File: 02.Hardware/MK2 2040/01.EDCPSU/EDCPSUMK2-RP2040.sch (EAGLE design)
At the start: 185 parts, among them J1 DX07S016JA1R1500, J6 Display, K1 FLEX CONNECTORES, Q2 2N7002PW, Q4 2N7002PW, Q5 2N7002PW, Q9 2N7002PW, U1 RP2040TR7, U10 IP2721, U11 AP63203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

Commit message: Añadido Test Pads
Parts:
- added 3V3MCU, EN_TPS54531, GND, GND_IN, IN+, ISENSE, N$41, N$51, N$59, OVC_ALARM, PEDAL+, PEDAL-, RUN, SCL, SDA, SEL, SWCLK, SWDIO, USB-D+, USB-D-, VBUS_SENSE, VOSEN, VOUT: TESTPAD_TPSQB1,27, BeagleBone_Blue_R3:TESTPAD_TPSQB1,27
- R35: value 330R -> 130R
- R36: value 75K -> 27K
- R51: value 220K -> 390K
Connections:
- net 3V3MCU: now also 3V3MCU.TP
- net EN_TPS54531: now also EN_TPS54531.TP
- net GND: now also GND.TP
- net GND_IN: now also GND_IN.TP
- net IN+: now also IN+.TP
- net ISENSE: now also ISENSE.TP
- net N$41: now also N$41.TP
- net N$51: now also N$51.TP
- net N$59: now also N$59.TP
- net OVC_ALARM: now also OVC_ALARM.TP
- net PEDAL+: now also PEDAL+.TP
- net PEDAL-: now also PEDAL-.TP
- net RUN: now also RUN.TP
- net SCL: now also SCL.TP
- net SDA: now also SDA.TP
- net SEL: now also SEL.TP
- net SWCLK: now also SWCLK.TP
- net SWDIO: now also SWDIO.TP
- net USB_D+: now also USB-D+.TP
- net USB_D-: now also USB-D-.TP
- net VBUS_SENSE: now also VBUS_SENSE.TP
- net VOSEN: now also VOSEN.TP
- net VOUT: now also VOUT.TP
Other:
- note added: "3V @ Vi=20V"
- note added: "3V @ Vi=25V"
- note added: "TEST PADS"
- note removed: "DIGITAL LDO + ROUTING + ISENSING"
- note removed: "Ratio= 1/5 5V @ Vi=25V"
- moved on the sheet: JP1

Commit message: Version 2 revisada de la EDCPSU
Los cambios son referidos a los issues #5, #6, #7, #8, #9, #10, #11, #12.
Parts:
- D3: value BAV199 -> N.C
- FB_ADJ: value JUMPER-SMT_2_NO_NO-SILK -> JUMPER-SMT_2_NC_TRACE_NO-SILK; device SparkFun-Jumpers:JUMPER-SMT_2_NO_NO-SILK -> SparkFun-Jumpers:JUMPER-SMT_2_NC_TRACE_NO-SILK
- R11: value 10K -> 15K
- R12: value 0.05R / 1W -> 0.025R / 1W
- R15: value N.C -> 0
- R41: value 330K -> 150K
- R43: value 27K -> 11K
- R57: value 800R -> 1K
- U8: value LM4040C25FTA -> LM4040C30FTA; device LM4040C25FTA:LM4040C25FTA -> LM4040C30FTA:LM4040C30FTA
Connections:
- removed net VCC-ISO: C15.1, C8.2, U5.VCC
- net 3V3MCU: now also C15.1, C8.2, U5.VCC
- net QSPI_SD0: now also U5.DI(IO0); no longer U5.DO(IO1)
- net QSPI_SD1: now also U5.DO(IO1); no longer U5.DI(IO0)
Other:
- note added: "MK2-RP2040 v2-May-2023"
- note removed: "MK2-RP2040 v1-March-2023"

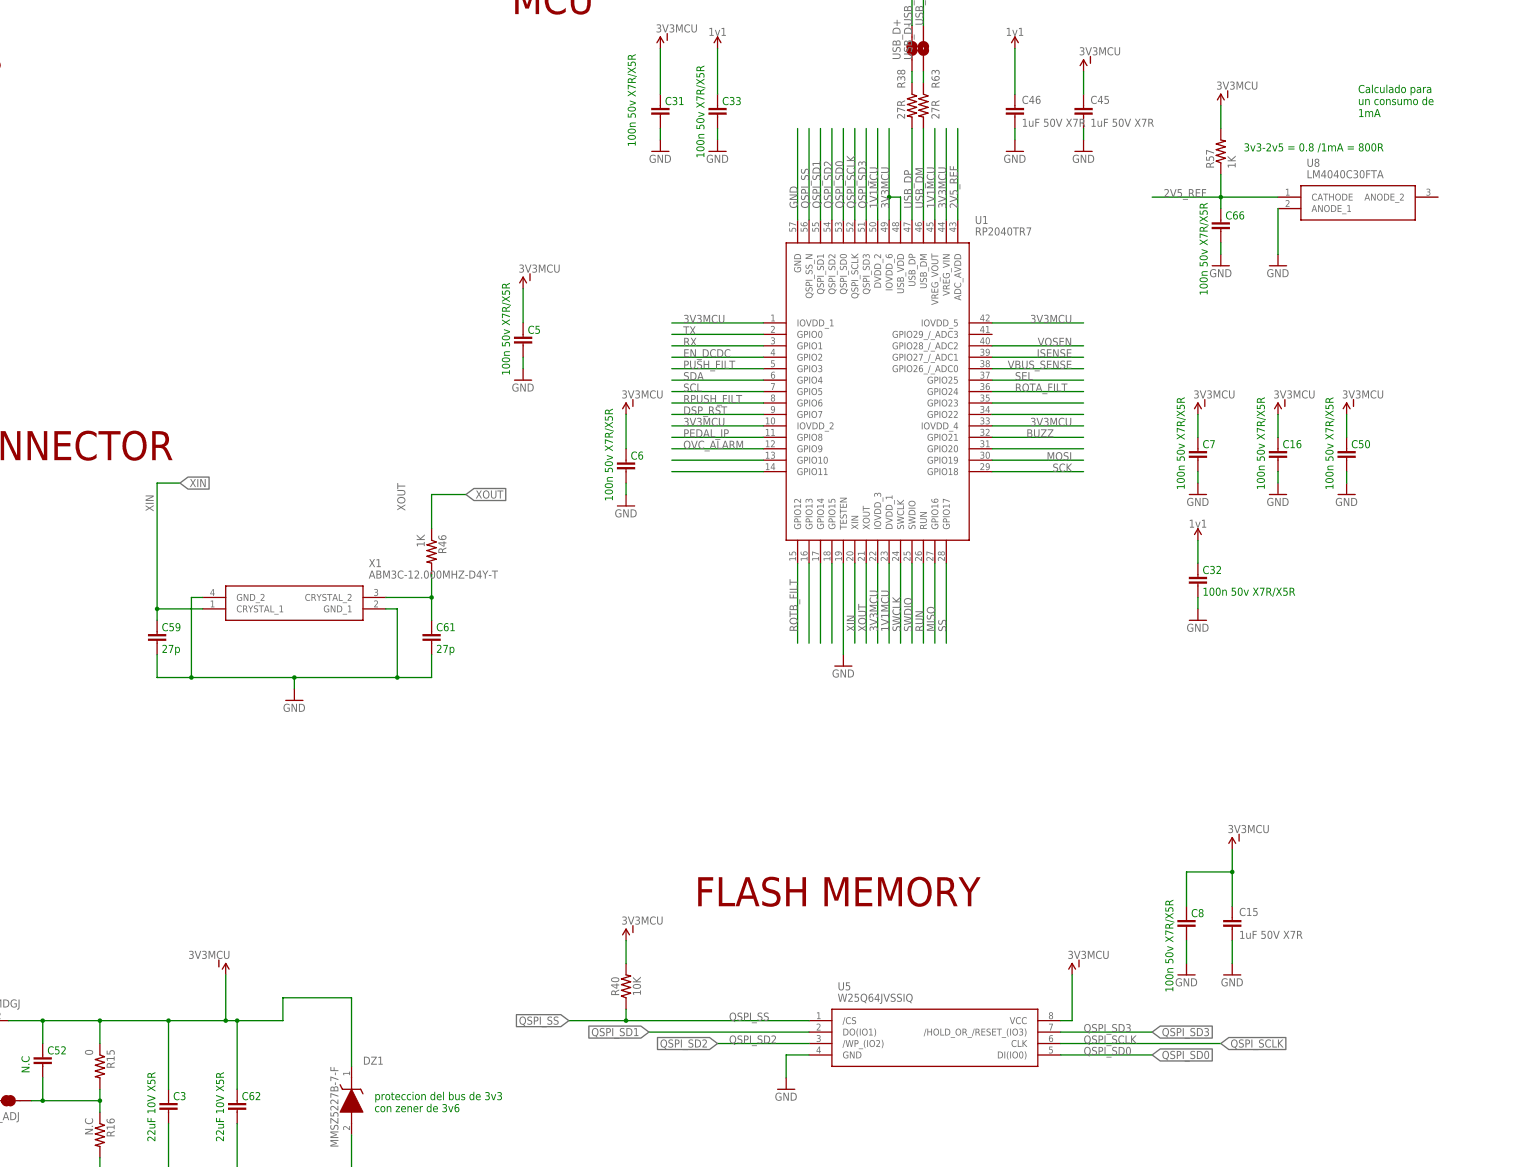
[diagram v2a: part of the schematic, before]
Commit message: Actualizacion de Cambios menores
R15 con valor 0R.
Lineas de Ref de tension a 3V_REF y R57 ajustada a 330R #10
Aumento de la linea de potencia de GND en la zona de la faja.
Mejora del marcaje de la colocacion de los Diodos.
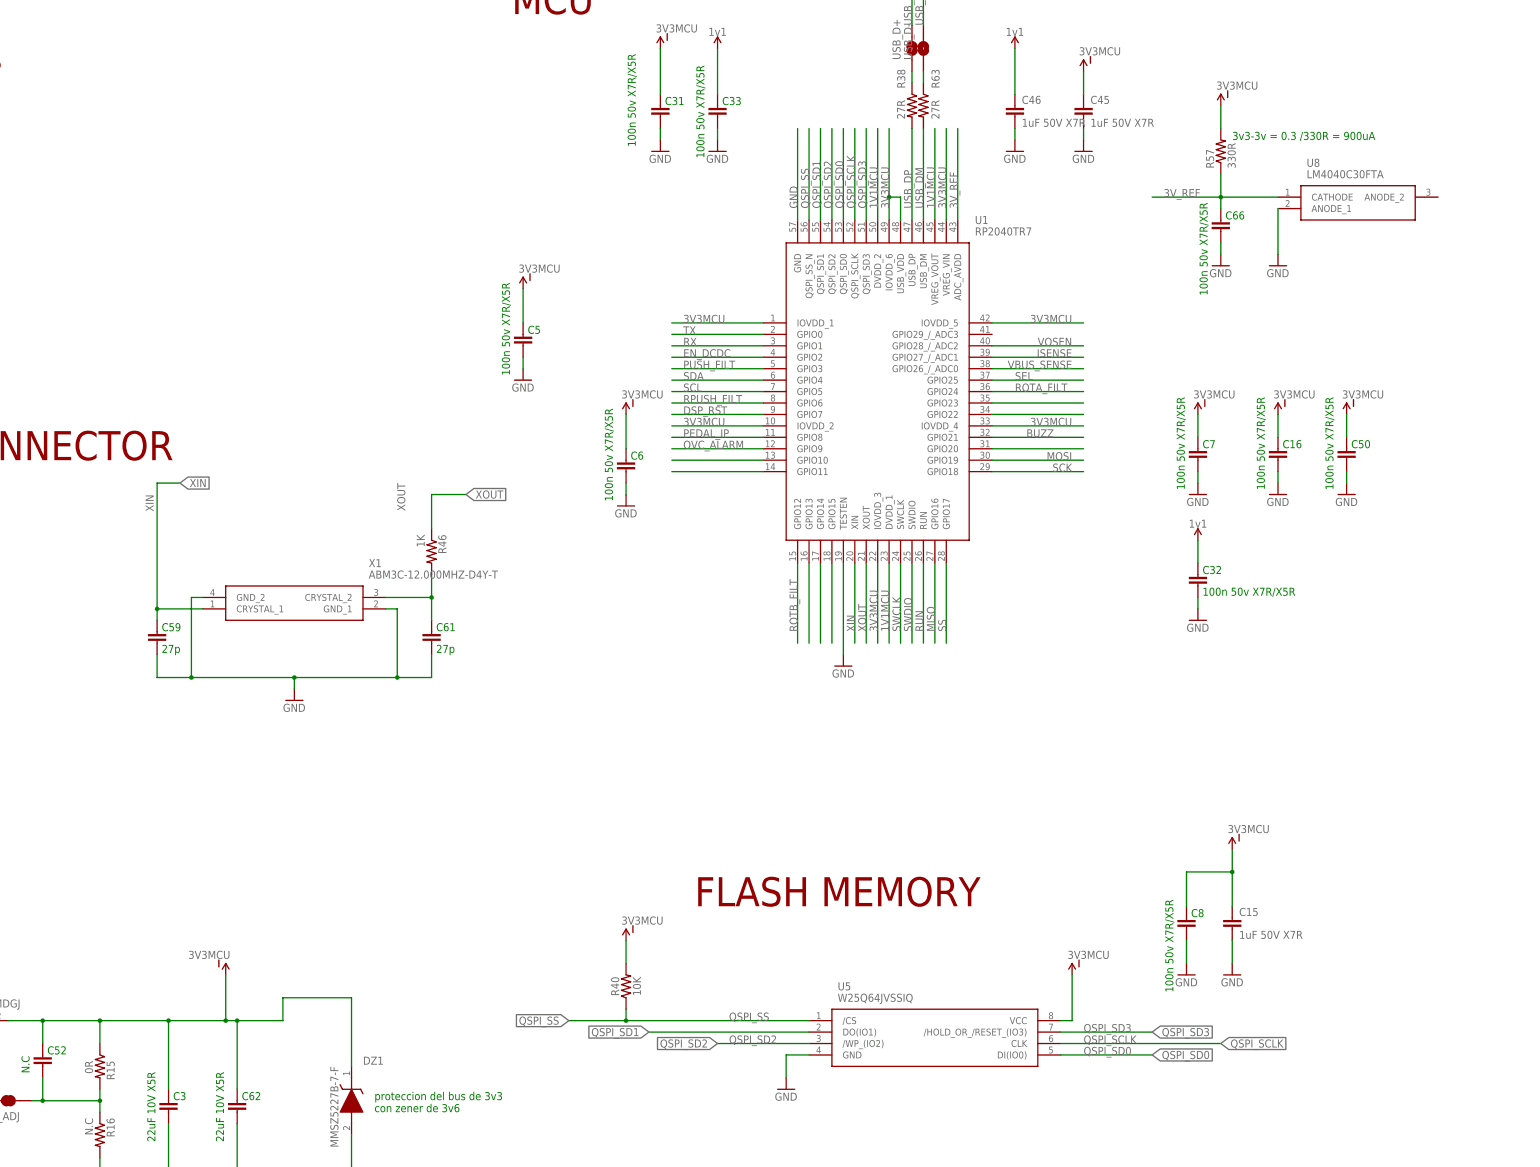
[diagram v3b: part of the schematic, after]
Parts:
- R15: value 0 -> 0R
- R57: value 1K -> 330R
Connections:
- net 2V5_REF renamed 3V_REF
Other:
- note added: "3v3-3v = 0.3 /330R = 900uA"
- note removed: "3v3-2v5 = 0.8 /1mA = 800R"
- note removed: "Calculado para un consumo de 1mA"
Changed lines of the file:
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@@
 <part name="GND61" library="SparkFun" deviceset="GND" device=""/>
 <part name="P+1" library="microbuilder" deviceset="VCC" device=""/>
-<part name="R15" library="SparkFun-Resistors" library_urn="urn:adsk.eagle:library:532" deviceset="RESISTOR" device="0805" package3d_urn="urn:adsk.eagle:package:39651/1" value="0"/>
+<part name="R15" library="SparkFun-Resistors" library_urn="urn:adsk.eagle:library:532" deviceset="RESISTOR" device="0805" package3d_urn="urn:adsk.eagle:package:39651/1" value="0R"/>
 <part name="C3" library="SparkFun-Passives" deviceset="CAP" device="0805" value="22uF 10V X5R"/>
 <part name="R16" library="SparkFun-Resistors" library_urn="urn:adsk.eagle:library:532" deviceset="RESISTOR" device="0805" package3d_urn="urn:adsk.eagle:package:39651/1" value="N.C"/>
@@
 <part name="GND82" library="SparkFun" deviceset="GND" device=""/>
 <part name="U$38" library="SparkFun-Aesthetics" deviceset="VCC-ISO" device="" value="3V3MCU"/>
-<part name="R57" library="SparkFun-Resistors" library_urn="urn:adsk.eagle:library:532" deviceset="RESISTOR" device="0805" package3d_urn="urn:adsk.eagle:package:39651/1" value="1K"/>
+<part name="R57" library="SparkFun-Resistors" library_urn="urn:adsk.eagle:library:532" deviceset="RESISTOR" device="0805" package3d_urn="urn:adsk.eagle:package:39651/1" value="330R"/>
 <part name="U12" library="AP64501SP-13" deviceset="AP64501SP-13" device=""/>
 <part name="U$39" library="SparkFun-Aesthetics" deviceset="VCC-ISO" device="" value="3V3MCU"/>
@@
 <text x="464.82" y="259.08" size="1.778" layer="91">Indicar esta referencia en el part number
 TLRP3A30CR050FTE</text>
-<text x="-78.74" y="274.32" size="1.778" layer="91">Calculado para
-un consumo de
-1mA
-</text>
-<text x="-104.14" y="266.7" size="1.778" layer="91">3v3-2v5 = 0.8 /1mA = 800R</text>
+<text x="-106.68" y="269.24" size="1.778" layer="91">3v3-3v = 0.3 /330R = 900uA</text>
 <text x="-233.68" y="7.62" size="1.778" layer="91">TVS
 ESD Protection Data</text>
@@
 </instance>
 <instance part="R15" gate="G$1" x="-358.14" y="63.5" smashed="yes" rot="R270">
-<attribute name="NAME" x="-356.6414" y="67.31" size="1.778" layer="95" rot="R270"/>
-<attribute name="VALUE" x="-361.442" y="67.31" size="1.778" layer="96" rot="R270"/>
+<attribute name="NAME" x="-356.6414" y="64.77" size="1.778" layer="95" rot="R270"/>
+<attribute name="VALUE" x="-361.442" y="64.77" size="1.778" layer="96" rot="R270"/>
 </instance>
 <instance part="C3" gate="G$1" x="-342.9" y="55.88" smashed="yes" rot="R180">
@@
 </segment>
 </net>
-<net name="2V5_REF" class="0">
+<net name="3V_REF" class="0">
 <segment>
 <pinref part="U8" gate="G$1" pin="CATHODE"/>

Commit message: Update EDCPSUMK2-RP2040
Cambio del Zener del 3,6v a 3,9v. #13
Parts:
- DZ1: value MMSZ5227B-7-F -> MMSZ5228B-7-F; device MMSZ5227B-7-F:MMSZ5227B-7-F -> MMSZ5228B-7-F:MMSZ5228B-7-F
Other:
- note added: "proteccion del bus de 3v3 con zener de 3v9"
- note removed: "proteccion del bus de 3v3 con zener de 3v6"
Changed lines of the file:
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@@
 <part name="C64" library="SparkFun-Passives" deviceset="CAP" device="0805" value="4.7uF 50V X5R"/>
 <part name="GND67" library="SparkFun" deviceset="GND" device=""/>
-<part name="DZ1" library="MMSZ5227B-7-F" deviceset="MMSZ5227B-7-F" device=""/>
+<part name="DZ1" library="MMSZ5228B-7-F" deviceset="MMSZ5228B-7-F" device=""/>
 <part name="U5" library="W25Q64JVSSIQ" deviceset="W25Q64JVSSIQ" device=""/>
 <part name="C8" library="SparkFun-Passives" deviceset="CAP" device="0805" value="100n 50v X7R/X5R"/>
@@
 U9 esta referenciado a GND_IN para
 poder sensar la caida en RSENSE.</text>
-<text x="-297.18" y="53.34" size="1.778" layer="91">proteccion del bus de 3v3
-con zener de 3v6</text>
+<text x="-297.18" y="53.34" size="1.778" layer="91">
+proteccion del bus de 3v3
+con zener de 3v9</text>
 <text x="-71.12" y="20.32" size="1.778" layer="91">Linea de corte en PCB</text>
 <text x="-337.82" y="-58.42" size="1.778" layer="91">3V @ Vi=20V</text>

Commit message: Update EDCPSUMK2-RP2040 - Diodo entrada D1
Cambio del diodo D1 de bidireccional a Unidireccional de 24v. #14
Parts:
- D1: value SMAJ24CA -> SMAJ24A; device SMAJ24CA:SMAJ24CA -> 3SMAJ5934B:3SMAJ5934B
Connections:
- net GND_IN: now also D1.A; no longer D1.1
- net IN+: now also D1.K; no longer D1.2
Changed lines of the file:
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@@
 <part name="P+3" library="microbuilder" deviceset="VCC" device=""/>
 <part name="D4" library="PESD5V0U2BT_215" deviceset="PESD5V0U2BT,215" device=""/>
-<part name="D1" library="SMAJ24CA" deviceset="SMAJ24CA" device=""/>
 <part name="R30" library="SparkFun-Resistors" library_urn="urn:adsk.eagle:library:532" deviceset="RESISTOR" device="0805" package3d_urn="urn:adsk.eagle:package:39651/1" value="N.C"/>
 <part name="R45" library="SparkFun-Resistors" library_urn="urn:adsk.eagle:library:532" deviceset="RESISTOR" device="0805" package3d_urn="urn:adsk.eagle:package:39651/1" value="N.C"/>
@@
 <part name="SDA" library="BeagleBone_Blue_R3" deviceset="TESTPAD_TPSQ" device="B1,27"/>
 <part name="SEL" library="BeagleBone_Blue_R3" deviceset="TESTPAD_TPSQ" device="B1,27"/>
+<part name="D1" library="3SMAJ5934B" deviceset="3SMAJ5934B" device="" value="SMAJ24A"/>
 </parts>
 <sheets>
@@
 <attribute name="VALUE" x="-201.93" y="7.62" size="1.778" layer="96" align="center-left"/>
 </instance>
-<instance part="D1" gate="G$1" x="-182.88" y="-38.1" smashed="yes" rot="R90">
-<attribute name="NAME" x="-189.23" y="-35.56" size="1.778" layer="95" rot="R90"/>
-<attribute name="VALUE" x="-186.69" y="-35.56" size="1.778" layer="96" rot="R90"/>
-</instance>
 <instance part="R30" gate="G$1" x="447.04" y="180.34" smashed="yes" rot="R180">
 <attribute name="NAME" x="448.31" y="183.9214" size="1.778" layer="95" rot="R180"/>
@@
 <attribute name="TP_SIGNAL_NAME" x="-354.88" y="355.5988" size="1.778" layer="97" rot="R270"/>
 </instance>
+<instance part="D1" gate="G$1" x="-175.26" y="-27.94" smashed="yes" rot="R90">
+<attribute name="NAME" x="-177.8" y="-25.4" size="1.778" layer="95" rot="R180"/>
+<attribute name="VALUE" x="-177.8" y="-29.21" size="1.778" layer="96" rot="R180"/>
+</instance>
 </instances>
 <busses>
@@
 </segment>
 <segment>
-<pinref part="D1" gate="G$1" pin="1"/>
-<label x="-170.18" y="-35.56" size="1.778" layer="95" rot="R180"/>
+<label x="-185.42" y="-35.56" size="1.778" layer="95" rot="R180"/>
 <pinref part="J1" gate="G$1" pin="SHIELD"/>
 <wire x1="-198.12" y1="-35.56" x2="-195.58" y2="-35.56" width="0.1524" layer="91"/>
@@
 <wire x1="-198.12" y1="-38.1" x2="-195.58" y2="-38.1" width="0.1524" layer="91"/>
 <pinref part="C56" gate="G$1" pin="2"/>
-<wire x1="-195.58" y1="-38.1" x2="-187.96" y2="-38.1" width="0.1524" layer="91"/>
-<wire x1="-177.8" y1="-38.1" x2="-167.64" y2="-38.1" width="0.1524" layer="91"/>
+<wire x1="-195.58" y1="-38.1" x2="-175.26" y2="-38.1" width="0.1524" layer="91"/>
+<wire x1="-175.26" y1="-38.1" x2="-167.64" y2="-38.1" width="0.1524" layer="91"/>
 <wire x1="-167.64" y1="-33.02" x2="-167.64" y2="-38.1" width="0.1524" layer="91"/>
 <junction x="-167.64" y="-38.1"/>
@@
 <wire x1="-195.58" y1="-35.56" x2="-195.58" y2="-38.1" width="0.1524" layer="91"/>
 <junction x="-195.58" y="-38.1"/>
-<wire x1="-187.96" y1="-38.1" x2="-187.96" y2="-43.18" width="0.1524" layer="91"/>
-<wire x1="-187.96" y1="-43.18" x2="-182.88" y2="-43.18" width="0.1524" layer="91"/>
-<wire x1="-182.88" y1="-43.18" x2="-177.8" y2="-43.18" width="0.1524" layer="91"/>
-<wire x1="-177.8" y1="-43.18" x2="-177.8" y2="-38.1" width="0.1524" layer="91"/>
-<wire x1="-182.88" y1="-38.1" x2="-182.88" y2="-43.18" width="0.1524" layer="91"/>
-<junction x="-182.88" y="-43.18"/>
+<junction x="-175.26" y="-38.1"/>
 <wire x1="-167.64" y1="-38.1" x2="-167.64" y2="-48.26" width="0.1524" layer="91"/>
 <wire x1="-167.64" y1="-48.26" x2="-152.4" y2="-48.26" width="0.1524" layer="91"/>
 <label x="-152.4" y="-48.26" size="1.778" layer="95" xref="yes"/>
+<pinref part="D1" gate="G$1" pin="A"/>
+<wire x1="-175.26" y1="-33.02" x2="-175.26" y2="-38.1" width="0.1524" layer="91"/>
 </segment>
 <segment>
@@
 </segment>
 <segment>
-<pinref part="D1" gate="G$1" pin="2"/>
 <pinref part="J1" gate="G$1" pin="VBUS"/>
-<wire x1="-198.12" y1="-20.32" x2="-187.96" y2="-20.32" width="0.1524" layer="91"/>
+<wire x1="-198.12" y1="-20.32" x2="-175.26" y2="-20.32" width="0.1524" layer="91"/>
 <label x="-195.58" y="-20.32" size="1.778" layer="95"/>
 <pinref part="C56" gate="G$1" pin="1"/>
-<wire x1="-177.8" y1="-20.32" x2="-167.64" y2="-20.32" width="0.1524" layer="91"/>
+<wire x1="-175.26" y1="-20.32" x2="-167.64" y2="-20.32" width="0.1524" layer="91"/>
 <wire x1="-167.64" y1="-25.4" x2="-167.64" y2="-20.32" width="0.1524" layer="91"/>
 <junction x="-167.64" y="-20.32"/>
@@
 <junction x="-45.72" y="-5.08"/>
 <wire x1="-66.04" y1="-5.08" x2="-45.72" y2="-5.08" width="0.1524" layer="91"/>
-<wire x1="-187.96" y1="-20.32" x2="-187.96" y2="-15.24" width="0.1524" layer="91"/>
-<wire x1="-187.96" y1="-15.24" x2="-182.88" y2="-15.24" width="0.1524" layer="91"/>
-<wire x1="-182.88" y1="-15.24" x2="-177.8" y2="-15.24" width="0.1524" layer="91"/>
-<wire x1="-177.8" y1="-15.24" x2="-177.8" y2="-20.32" width="0.1524" layer="91"/>
-<wire x1="-182.88" y1="-15.24" x2="-182.88" y2="-17.78" width="0.1524" layer="91"/>
-<junction x="-182.88" y="-15.24"/>
+<junction x="-175.26" y="-20.32"/>
 <label x="-68.58" y="5.08" size="1.778" layer="95" rot="R180" xref="yes"/>
 <wire x1="-68.58" y1="5.08" x2="-66.04" y2="5.08" width="0.1524" layer="91"/>
 <wire x1="-66.04" y1="5.08" x2="-66.04" y2="-5.08" width="0.1524" layer="91"/>
 <junction x="-66.04" y="-5.08"/>
+<pinref part="D1" gate="G$1" pin="K"/>
+<wire x1="-175.26" y1="-22.86" x2="-175.26" y2="-20.32" width="0.1524" layer="91"/>
 </segment>
 <segment>
